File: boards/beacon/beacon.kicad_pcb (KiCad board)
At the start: 2 copper layers, 33 x 61.5 mm, 20 parts, among them J2 Conn_01x02_Pin, J3 Conn_01x02_Pin, J4 Conn_01x05_Pin, J5 Conn_01x03_Pin, U1 SAM-M8Q, U2 RFM96W-433S2, U3 ATmega328PB-A, U4 LM3670MF, Y1 Crystal

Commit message: pcb organization done for now, tracing asap
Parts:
- moved C3 125.9 mm to (102.0, 109.0), turned to 180 degrees
- moved C2 124.1 mm to (101.0, 93.5), turned to 90 degrees
- moved Y1 120.8 mm to (105.0, 101.0), turned to 90 degrees
- moved R3 105.9 mm to (123.1, 91.5)
- moved R2 105.7 mm to (123.0, 86.5)
- moved R1 105.4 mm to (123.0, 81.5)
- moved C1 103.8 mm to (127.5, 109.0), turned to 180 degrees
- moved SW_RESET1 100.8 mm to (127.8, 101.0), turned to -90 degrees
- moved J2 95.3 mm to (137.0, 75.7)
- moved U4 79.6 mm to (126.1, 70.0)
- moved C4 78.4 mm to (123.0, 66.0), turned to 180 degrees
- moved L1 77.1 mm to (130.0, 66.0)
- moved C5 74.5 mm to (126.0, 75.0), turned to 180 degrees
- moved J3 68.0 mm to (137.0, 66.2)
- moved J5 64.3 mm to (137.0, 85.5)
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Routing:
- net Net-(U3-XTAL1/PB6): track 0.00 -> 15.4 mm
- net Net-(U3-XTAL2/PB7): track 0.00 -> 10.7 mm

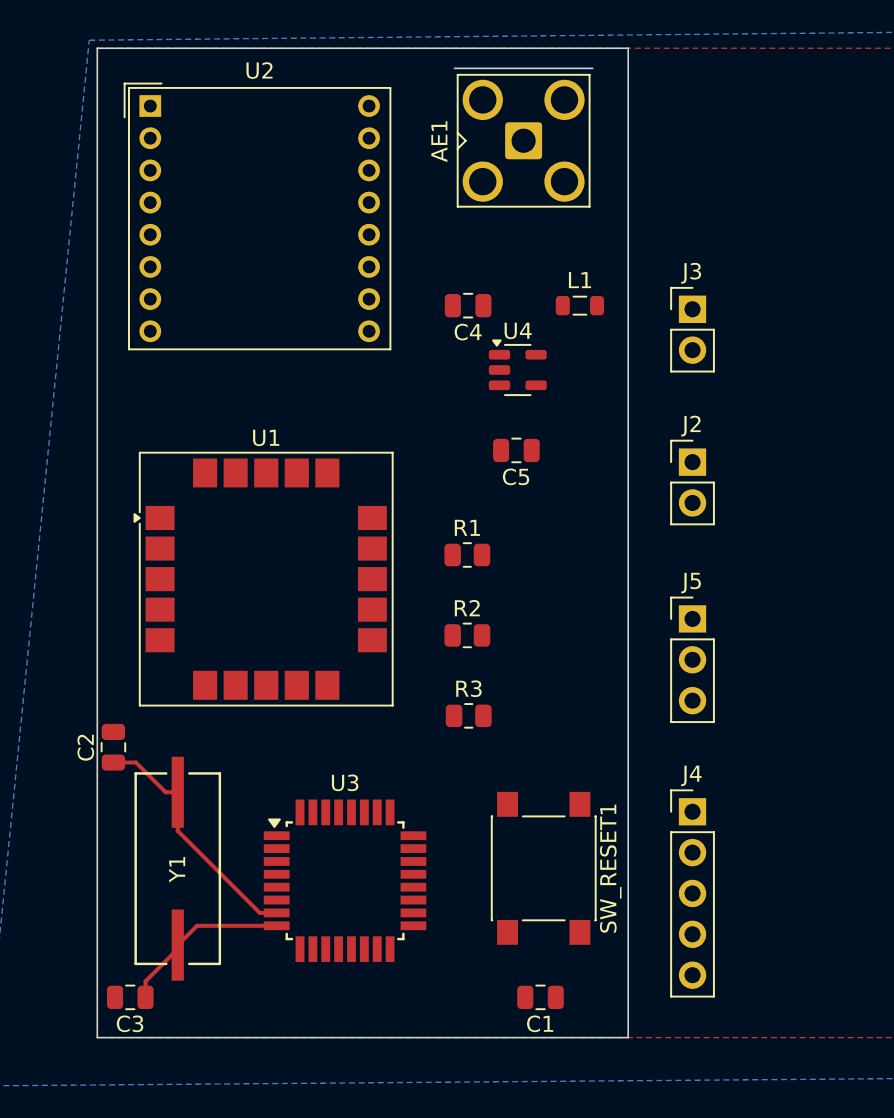
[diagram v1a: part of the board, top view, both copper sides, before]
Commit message: some starter traces
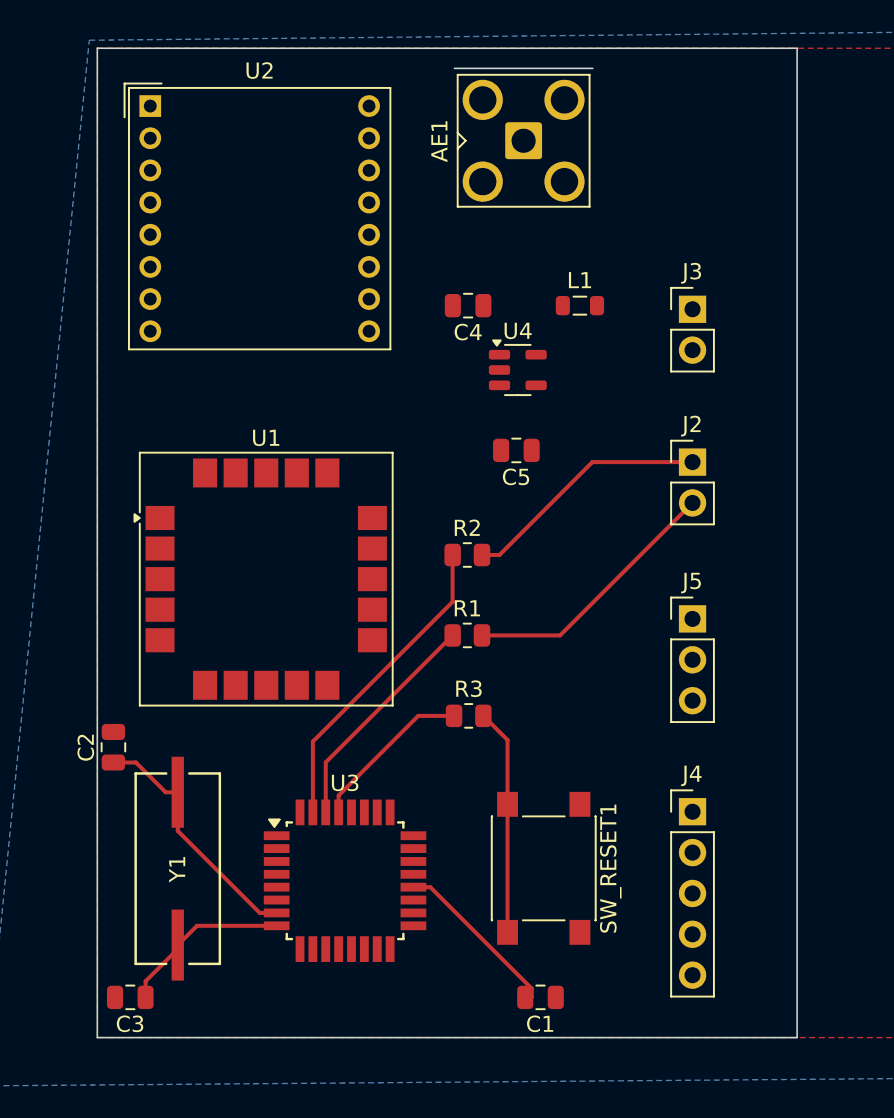
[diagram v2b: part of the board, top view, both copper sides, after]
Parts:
- moved R1 5.00 mm to (123.0, 86.5)
- moved R2 5.00 mm to (123.0, 81.5)
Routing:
- net /mcu/TX: track 0.00 -> 19.6 mm
- net Net-(J2-Pin_2): track 0.00 -> 16.5 mm
- net Net-(J2-Pin_1): track 0.00 -> 15.5 mm
- net /mcu/RX: track 0.00 -> 14.3 mm
- net Net-(R3-Pad2): track 0.00 -> 14.1 mm
- net Net-(U3-AREF): track 0.00 -> 10.9 mm
- net /mcu/RESET: track 0.00 -> 10.3 mm
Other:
- board size 33 x 61.5 mm -> 43.5 x 61.5 mm
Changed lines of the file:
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@@
 	(footprint "Resistor_SMD:R_0805_2012Metric"
 		(layer "F.Cu")
-		(at 123 86.5)
+		(at 123 81.5)
 		(descr "Resistor SMD 0805 (2012 Metric), square (rectangular) end terminal, IPC_7351 nominal, (Body size source: IPC-SM-782 page 72, https://www.pcb-3d.com/wordpress/wp-content/uploads/ipc-sm-782a_amendment_1_and_2.pdf), generated with kicad-footprint-generator")
 		(tags "resistor")
@@
 	(footprint "Resistor_SMD:R_0805_2012Metric"
 		(layer "F.Cu")
-		(at 123 81.5)
+		(at 123 86.5)
 		(descr "Resistor SMD 0805 (2012 Metric), square (rectangular) end terminal, IPC_7351 nominal, (Body size source: IPC-SM-782 page 72, https://www.pcb-3d.com/wordpress/wp-content/uploads/ipc-sm-782a_amendment_1_and_2.pdf), generated with kicad-footprint-generator")
 		(tags "resistor")
@@
 	(gr_rect
 		(start 100 50)
-		(end 133 111.5)
+		(end 143.5 111.5)
 		(stroke
 			(width 0.1)
@@
 	)
 	(segment
+		(start 126.6 109)
+		(end 127 109)
+		(width 0.25)
+		(layer "F.Cu")
+		(net 2)
+	)
+	(segment
+		(start 127 109)
+		(end 127 108.45)
+		(width 0.25)
+		(layer "F.Cu")
+		(net 2)
+	)
+	(segment
+		(start 127 108.45)
+		(end 120.7 102.15)
+		(width 0.25)
+		(layer "F.Cu")
+		(net 2)
+	)
+	(segment
+		(start 120.7 102.15)
+		(end 119.65 102.15)
+		(width 0.25)
+		(layer "F.Cu")
+		(net 2)
+	)
+	(segment
 		(start 105 98.65)
 		(end 105 96.2502)
@@
 		(net 5)
 	)
+	(segment
+		(start 137 85.475)
+		(end 137 85.5)
+		(width 0.25)
+		(layer "B.Cu")
+		(net 6)
+	)
+	(segment
+		(start 123.9125 86.5)
+		(end 128.765 86.5)
+		(width 0.25)
+		(layer "F.Cu")
+		(net 8)
+	)
+	(segment
+		(start 128.765 86.5)
+		(end 137 78.265)
+		(width 0.25)
+		(layer "F.Cu")
+		(net 8)
+	)
+	(segment
+		(start 125 81.5)
+		(end 130.775 75.725)
+		(width 0.25)
+		(layer "F.Cu")
+		(net 9)
+	)
+	(segment
+		(start 123.9125 81.5)
+		(end 125 81.5)
+		(width 0.25)
+		(layer "F.Cu")
+		(net 9)
+	)
+	(segment
+		(start 130.775 75.725)
+		(end 137 75.725)
+		(width 0.25)
+		(layer "F.Cu")
+		(net 9)
+	)
+	(segment
+		(start 122.0875 86.5)
+		(end 114.2 94.3875)
+		(width 0.25)
+		(layer "F.Cu")
+		(net 16)
+	)
+	(segment
+		(start 114.2 94.3875)
+		(end 114.2 97.5)
+		(width 0.25)
+		(layer "F.Cu")
+		(net 16)
+	)
+	(segment
+		(start 122.0875 84.4125)
+		(end 113.4 93.1)
+		(width 0.25)
+		(layer "F.Cu")
+		(net 17)
+	)
+	(segment
+		(start 113.4 93.1)
+		(end 113.4 97.5)
+		(width 0.25)
+		(layer "F.Cu")
+		(net 17)
+	)
+	(segment
+		(start 122.0875 81.5)
+		(end 122.0875 84.4125)
+		(width 0.25)
+		(layer "F.Cu")
+		(net 17)
+	)
+	(segment
+		(start 125.5 97)
+		(end 125.5 104.96)
+		(width 0.25)
+		(layer "F.Cu")
+		(net 18)
+	)
+	(segment
+		(start 125.5 97)
+		(end 125.5 93)
+		(width 0.25)
+		(layer "F.Cu")
+		(net 18)
+	)
+	(segment
+		(start 125.5 93)
+		(end 124 91.5)
+		(width 0.25)
+		(layer "F.Cu")
+		(net 18)
+	)
+	(segment
+		(start 119.95 91.5)
+		(end 115 96.45)
+		(width 0.25)
+		(layer "F.Cu")
+		(net 19)
+	)
+	(segment
+		(start 115 96.45)
+		(end 115 97.5)
+		(width 0.25)
+		(layer "F.Cu")
+		(net 19)
+	)
+	(segment
+		(start 122.175 91.5)
+		(end 119.95 91.5)
+		(width 0.25)
+		(layer "F.Cu")
+		(net 19)
+	)
 	(zone

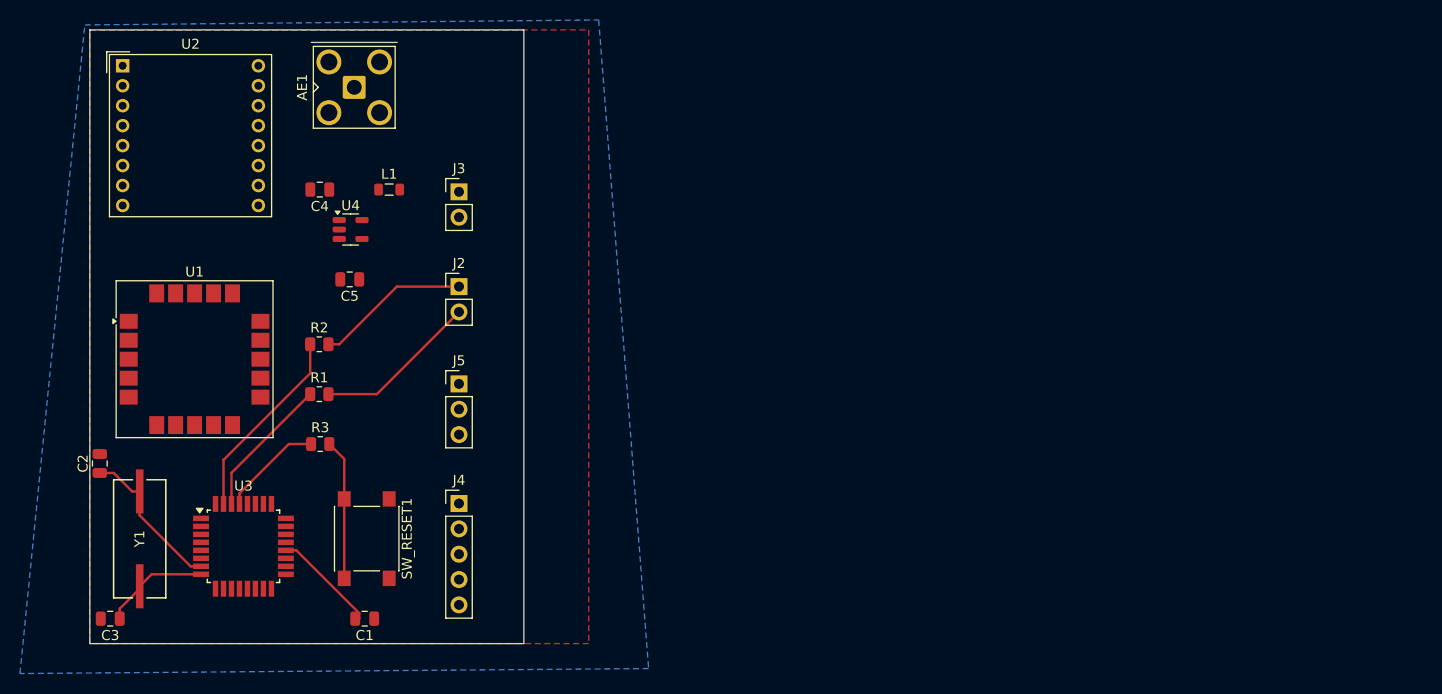
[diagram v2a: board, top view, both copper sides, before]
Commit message: beacon down to warnings only
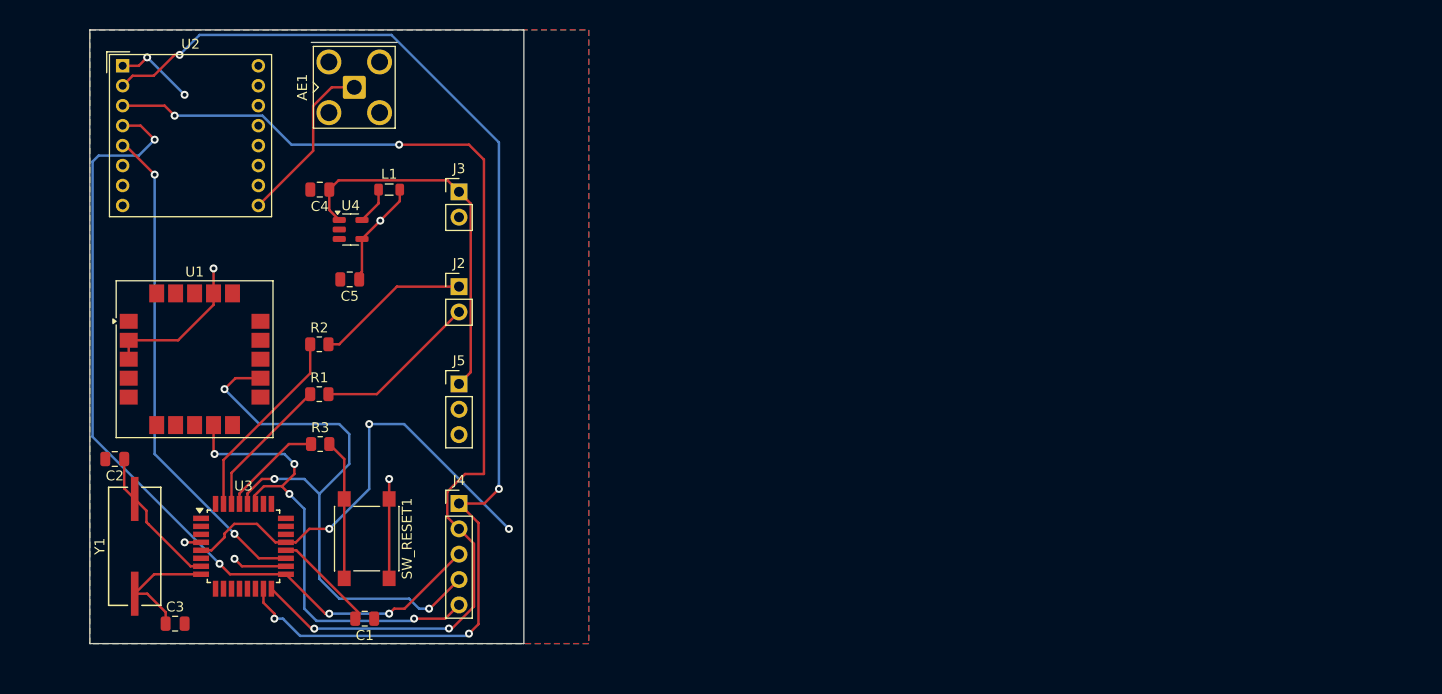
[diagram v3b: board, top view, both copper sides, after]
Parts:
- moved C3 6.52 mm to (108.5, 109.5), turned to 0 degrees
- moved C2 1.57 mm to (102.5, 93.0), turned to 180 degrees
- moved Y1 0.90 mm to (104.5, 101.7)
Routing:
- net /MISO: track 0.00 -> 122.2 mm, vias 0 -> 4
- net /MOSI: track 0.00 -> 109.9 mm, vias 0 -> 4
- net /SCK: track 0.00 -> 85.0 mm, vias 0 -> 4
- net /I2C_SCL: track 0.00 -> 60.1 mm, vias 0 -> 3
- net GND: track 0.00 -> 54.1 mm, vias 0 -> 5
- net /transceiver_CS: track 0.00 -> 49.9 mm, vias 0 -> 2
- net /I2C_SDA: track 0.00 -> 48.1 mm, vias 0 -> 4
- net +3.3V: track 0.00 -> 43.3 mm, vias 0 -> 5
- net INPUT_VOLTAGE: track 0.03 -> 37.6 mm
- net Net-(AE1-A): track 0.00 -> 17.1 mm
- net Net-(U4-SW): track 0.00 -> 3.74 mm
- net Net-(U3-XTAL2/PB7): track 10.7 -> 12.5 mm
- net Net-(U3-XTAL1/PB6): track 15.4 -> 14.6 mm
